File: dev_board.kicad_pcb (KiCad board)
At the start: 2 copper layers, 29 parts, among them J3 Conn_02x10_Odd_Even, J4 Conn_02x10_Odd_Even, U1 93LCxxB, U2 LT8609, U3 KSZ8081RND

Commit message: a bunch of stuff I guess. mostly layout.
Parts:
- removed C1: 1uF, Capacitors_SMD:C_0603
- added C13: 0.1u, Capacitors_SMD:C_0603, F.Cu at (30.7, 102.0)
- added C14: 0.1u, Capacitors_SMD:C_0603, F.Cu at (79.2, 114.9)
- added C15: 22u, Capacitors_SMD:C_0603, F.Cu at (91.3, 85.5)
- added C16: 0.1u, Capacitors_SMD:C_0603, F.Cu at (82.1, 123.7)
- added C17: C_Small, Capacitors_SMD:C_0603, F.Cu at (123.4, 119.4)
- added C18: C_Small, Capacitors_SMD:C_0603, F.Cu at (121.9, 119.4)
- added C19: C_Small, Capacitors_SMD:C_0603, F.Cu at (122.7, 111.1)
- added C20: C_Small, Capacitors_SMD:C_0603, F.Cu at (122.8, 105.9)
- added C21: C_Small, Capacitors_SMD:C_0603, F.Cu at (114.8, 108.6)
- added C22: C_Small, Capacitors_SMD:C_0603, F.Cu at (110.8, 108.5)
- added C23: 100nF, Capacitors_SMD:C_0603, F.Cu at (83.9, 111.9)
- added C24: 100nF, Capacitors_SMD:C_0603, F.Cu at (79.5, 108.8)
- added C25: 100nF, Capacitors_SMD:C_0603, F.Cu at (85.3, 111.9)
- added C26: 100nF, Capacitors_SMD:C_0603, F.Cu at (80.4, 103.2)
- added C27: 100nF, Capacitors_SMD:C_0603, F.Cu at (92.5, 100.3)
- added C28: 4.7uF, Capacitors_SMD:C_0603, F.Cu at (83.9, 109.0)
- added C29: 10nF, Capacitors_SMD:C_0603, F.Cu at (82.6, 99.6)
- added C30: 1uF, Capacitors_SMD:C_0603, F.Cu at (85.3, 109.0)
- added C31: C_Small, Capacitors_SMD:C_0603, F.Cu at (85.7, 100.2)
- added C32: C_Small, Capacitors_SMD:C_0603, F.Cu at (93.6, 137.6)
- added J1: USB_B_Micro, Connectors_USB:USB_Micro-B_Molex-105017-0001, F.Cu at (111.9, 98.5)
- added J2: ARJ-169, Exodus_Connectors:ARJ-169, F.Cu at (38.3, 88.6)
- added L3: Ferrite_Bead_Small, Inductors_SMD:L_0603, F.Cu at (114.8, 106.9)
- added L4: Ferrite_Bead_Small, Inductors_SMD:L_0603, F.Cu at (110.8, 106.8)
- added R12: 1M DNP, Resistors_SMD:R_0603, F.Cu at (30.5, 103.4)
- added R13: 6.49K 1%, Resistors_SMD:R_0603, F.Cu at (89.9, 85.3)
- added R14: R_Small, Resistors_SMD:R_0603, F.Cu at (119.8, 116.4)
- added R15: R_Small, Resistors_SMD:R_0603, F.Cu at (114.0, 122.7)
- added R16: R_Small, Resistors_SMD:R_0603, F.Cu at (114.8, 105.3)
- added SW1: SW_Push, Buttons_Switches_SMD:SW_SPST_EVPBF, F.Cu at (82.3, 85.7)
- added U4: FT232H, Housings_QFP:LQFP-48_7x7mm_Pitch0.5mm, F.Cu at (112.3, 115.6)
- added U5: STM32F107RCTx, Housings_QFP:LQFP-64_10x10mm_Pitch0.5mm, F.Cu at (69.9, 107.6)
- C10: value 0.1u -> 47u
- C12: value 0.1u -> 22u
- C2: value 4.7uF -> 1uF
- C3: value 10nF -> C_Small
- C5: value 10pF -> 0.1uF
- C6: value 22uF -> 2.2u
- C7: value 22u -> 330p
- L1: value 2.2uH -> 1u; footprint Inductors_SMD:L_Vishay_IHLP-2020 -> Inductors_SMD:L_Vishay_IHLP-1616
- R1: value 18.2k -> 10k
- R10: value 10K -> 1K
- R11: value 1M DNP -> 10K
- R2: value 309k -> 20k
- R3: value 1M -> 324k
- R4: value 100k -> 115k
- R5: value 1K -> 25.5
- R6: value 1M DNP -> 1K
- R7: value 1K -> 1M DNP
- R8: value 10K DNP -> 1K
- R9: value 1K -> 10K DNP
- U1: value 93LCxxB -> LTC3604_UD; footprint Housings_QFP:LQFP-52_10x10mm_Pitch0.65mm -> Housings_DFN_QFN:QFN-16-1EP_3x3mm_Pitch0.5mm_ThermalVias
- U2: value LT8609 -> KSZ8081RND; footprint Housings_SSOP:MSOP-10-1EP_3x3mm_Pitch0.5mm -> Housings_DFN_QFN:QFN-24-1EP_4x4mm_Pitch0.5mm
- U3: value KSZ8081RND -> 93LCxxB; footprint Housings_DFN_QFN:QFN-20-1EP_4x4mm_Pitch0.5mm -> Housings_SOIC:SOIC-8_3.9x4.9mm_Pitch1.27mm
- moved J3 126.4 mm to (36.4, 109.7)
- moved R6 107.5 mm to (59.6, 85.6)
- moved R7 96.3 mm to (72.1, 90.0)
- moved R9 95.6 mm to (69.5, 87.9)
- moved C12 90.3 mm to (59.2, 96.8)
- moved R11 88.0 mm to (71.8, 94.0)
- moved R10 85.5 mm to (73.7, 87.4)
- moved C11 84.5 mm to (59.4, 93.1)
- moved R8 80.9 mm to (59.1, 107.2)
- moved R3 65.4 mm to (130.3, 57.5)
- moved C3 65.3 mm to (62.4, 130.8), turned to 90 degrees
- moved C5 60.1 mm to (71.6, 132.2), turned to 180 degrees
- moved R1 58.8 mm to (67.7, 127.3), turned to 90 degrees
- moved R5 57.8 mm to (130.3, 56.0)
- moved C6 57.5 mm to (133.3, 60.7)
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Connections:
- net /ethernet_phy_ksz8081/TXP renamed Net-(U3-Pad6)
- net Net-(U1-Pad2) renamed /power_supply/PGOOD
- C10 pad 1: /ethernet_phy_ksz8081/1.2V_INTERNALLY_REGULATED -> +3V3
- C11 pad 1: +3V3 -> /ethernet_phy_ksz8081/3.3V_QUIET
- C12 pad 1: +3V3 -> /ethernet_phy_ksz8081/1.2V_INTERNALLY_REGULATED
- C2 pad 1: +5V -> GND
- C2 pad 2: GND -> +5V
- C3 pad 1: Net-(C3-Pad1) -> /NRST
- C4 pad 2: Net-(C4-Pad2) -> GND
- C5 pad 1: +3V3 -> Net-(C5-Pad1)
- C5 pad 2: Net-(C5-Pad2) -> GND
- C6 pad 1: +3V3 -> /power_supply/INTVcc
- C7 pad 1: /ethernet_phy_ksz8081/3.3V_QUIET -> Net-(C7-Pad1)
- C8 pad 1: /ethernet_phy_ksz8081/1.2V_INTERNALLY_REGULATED -> +5V
- C9 pad 1: /ethernet_phy_ksz8081/3.3V_QUIET -> /power_supply/BST
- C9 pad 2: GND -> /power_supply/SW
- J3 pad 1: Net-(J3-Pad1) -> +3V3
- J3 pad 2: Net-(J3-Pad2) -> +5V
- J3 pad 3: Net-(J3-Pad3) -> GND
- J3 pad 4: Net-(J3-Pad4) -> GND
- J4 pad 1: Net-(J4-Pad1) -> +3V3
- J4 pad 2: Net-(J4-Pad2) -> +5V
- J4 pad 3: Net-(J4-Pad3) -> GND
- J4 pad 4: Net-(J4-Pad4) -> GND
- L1 pad 1: Net-(C4-Pad1) -> /power_supply/SW
- R1 pad 1: Net-(R1-Pad1) -> +3V3
- R1 pad 2: GND -> /NRST
- R10 pad 1: /ethernet_phy_ksz8081/RMII_RXER -> /stm32f107/ETH_RMII_CRS_DV
- R11 pad 1: /ethernet_phy_ksz8081/RMII_TXEN -> /ethernet_phy_ksz8081/RMII_RXER
- R2 pad 1: Net-(C5-Pad2) -> /power_supply/ITH
- R2 pad 2: GND -> Net-(C7-Pad1)
- R3 pad 1: +3V3 -> /power_supply/RT
- R3 pad 2: Net-(C5-Pad2) -> GND
- R4 pad 2: /power_supply/P_GOOD -> /power_supply/FB
- R5 pad 1: +3V3 -> /power_supply/FB
- R5 pad 2: /ethernet_phy_ksz8081/RMII_MDIO -> GND
- R6 pad 2: /ethernet_phy_ksz8081/RMII_MDC -> /stm32f107/ETH_RMII_MDIO
- R7 pad 2: /ethernet_phy_ksz8081/INTRP -> /stm32f107/ETH_RMII_MDC
- R8 pad 2: /NRST -> /ethernet_phy_ksz8081/INTRP
- R9 pad 1: /ethernet_phy_ksz8081/RMII_CRS_DV -> +3V3
- R9 pad 2: GND -> /NRST
- U1 pad 10: (no net) -> /power_supply/RT
- U1 pad 11: (no net) -> /power_supply/FB
- U1 pad 12: (no net) -> /power_supply/ITH
- U1 pad 13: (no net) -> Net-(U1-Pad13)
- U1 pad 14: (no net) -> +5V
- U1 pad 15: (no net) -> +5V
- U1 pad 16: (no net) -> +5V
- U1 pad 17: (no net) -> GND
- U1 pad 3: Net-(R14-Pad1) -> /power_supply/SW
- U1 pad 4: Net-(R14-Pad2) -> /power_supply/SW
- U1 pad 5: GND -> Net-(U1-Pad5)
- U1 pad 6: Net-(U1-Pad6) -> /power_supply/BST
- U1 pad 7: Net-(U1-Pad7) -> /power_supply/INTVcc
- U1 pad 9: (no net) -> GND
- U2 pad 1: Net-(C4-Pad2) -> /ethernet_phy_ksz8081/1.2V_INTERNALLY_REGULATED
- U2 pad 10: +5V -> /stm32f107/ETH_RMII_MDIO
- U2 pad 11: GND -> /stm32f107/ETH_RMII_MDC
- U2 pad 2: Net-(C4-Pad1) -> /ethernet_phy_ksz8081/3.3V_QUIET
- U2 pad 3: Net-(C1-Pad1) -> /RXM
- U2 pad 4: Net-(R1-Pad1) -> /RXP
- U2 pad 5: Net-(U2-Pad5) -> /TXM
- U2 pad 6: Net-(C5-Pad2) -> /TXP
- U2 pad 7: Net-(C3-Pad1) -> /ethernet_phy_ksz8081/OSC_OUT
- U2 pad 8: /power_supply/P_GOOD -> /stm32f107/MCO
- U2 pad 9: +5V -> /ethernet_phy_ksz8081/PHY_REF_RES
- U3 pad 1: /ethernet_phy_ksz8081/1.2V_INTERNALLY_REGULATED -> Net-(U3-Pad1)
- U3 pad 2: /ethernet_phy_ksz8081/3.3V_QUIET -> Net-(U3-Pad2)
- U3 pad 3: /ethernet_phy_ksz8081/RXM -> Net-(R14-Pad1)
- U3 pad 4: /ethernet_phy_ksz8081/RXP -> Net-(R14-Pad2)
- U3 pad 5: /ethernet_phy_ksz8081/TXM -> GND
- U3 pad 7: /ethernet_phy_ksz8081/OSC_OUT -> Net-(U3-Pad7)
- U3 pad 8: /ethernet_phy_ksz8081/REF_CLK_50MHZ -> +3V3
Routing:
- net +1V8: track 0.00 -> 10.3 mm
- net Net-(C20-Pad1): track 0.00 -> 10.2 mm
- net Net-(C19-Pad1): track 0.00 -> 8.61 mm
- net Net-(C18-Pad1): track 0.00 -> 8.00 mm
- net Net-(R14-Pad1): track 0.00 -> 5.89 mm
- net +3V3: track 0.00 -> 5.79 mm
- net Net-(C22-Pad1): track 0.00 -> 4.42 mm
- net Net-(C21-Pad2): track 0.00 -> 4.30 mm
- net Net-(U3-Pad1): track 0.00 -> 3.96 mm
- net Net-(U3-Pad2): track 0.00 -> 3.75 mm
- net Net-(R14-Pad2): track 0.00 -> 2.62 mm
- net Net-(R15-Pad1): track 0.00 -> 2.04 mm
- net /power_supply/RT: track 0.00 -> 1.74 mm
- net +5V: track 0.00 -> 1.00 mm
- net /USB_PROG_D+: track 0.00 -> 0.97 mm
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- added copper zone on F.Cu, net +3V3
- added copper zone on F.Cu, net +5V
- added copper zone on F.Cu, net /power_supply/BST
- added copper zone on F.Cu, net /power_supply/FB
- added copper zone on F.Cu, net /power_supply/INTVcc
- added copper zone on F.Cu, net /power_supply/ITH
- added copper zone on F.Cu, net /power_supply/SW
- added copper zone on B.Cu, net GND
- added copper zone on F.Cu, net GND
- added copper zone on F.Cu, net Net-(C7-Pad1)
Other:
- board outline added: 76.2 x 58.4 mm
- net class Default: clearance 0.2 -> 0.1524; trace_width 0.25 -> 0.1524; via_dia 0.8 -> 0.6858; via_drill 0.4 -> 0.3302
- rule pad_to_mask_clearance: 0.2 -> 0.0508
- rule trace_clearance: 0.2 -> 0.1524
- rule trace_min: 0.2 -> 0.1524
- rule via_min_drill: 0.3 -> 0.254
- rule via_min_size: 0.4 -> 0.508

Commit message: more layout
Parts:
- moved J3 110.2 mm to (144.5, 87.6)
- moved C13 53.3 mm to (77.0, 128.3)
- moved R12 53.3 mm to (76.8, 129.7)
- moved U2 38.4 mm to (76.9, 109.8), turned to 270 degrees
- moved J2 38.3 mm to (76.2, 83.2), turned to 180 degrees
- moved R13 36.8 mm to (68.5, 115.3)
- moved C15 36.8 mm to (69.9, 115.4)
- moved U1 31.1 mm to (118.8, 90.0)
- moved C10 31.1 mm to (123.3, 101.0)
- moved L1 31.1 mm to (123.7, 96.4)
- moved C6 31.1 mm to (123.1, 90.0)
- moved C7 31.1 mm to (116.9, 85.3)
- moved C8 31.1 mm to (116.8, 93.1)
- moved R2 31.1 mm to (117.0, 86.9)
- moved C9 31.1 mm to (122.4, 92.2)
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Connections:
- net /RXM renamed /RX_N
- net /RXP renamed /RX_P
- net /TXM renamed /TX_N
- net /TXP renamed /TX_P
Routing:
- net /stm32f107/ETH_RMII_TXD1: track 0.00 -> 14.7 mm
- net /stm32f107/ETH_RMII_TXD0: track 0.00 -> 13.6 mm
- net /TX_P: track 0.00 -> 11.3 mm
- net /RX_N: track 0.00 -> 11.2 mm
- net /stm32f107/ETH_RMII_TX_EN: track 0.00 -> 10.7 mm, vias 0 -> 2
- net /TX_N: track 0.00 -> 10.7 mm
- net /RX_P: track 0.00 -> 10.5 mm
- net /USB_PROG_D-: track 0.76 -> 10.4 mm
- net /USB_PROG_D+: track 0.97 -> 10.5 mm
- net Net-(R16-Pad1): track 0.00 -> 6.60 mm
- net +3V3: track 5.79 -> 2.85 mm
- net /stm32f107/ETH_RMII_RXD0: track 0.65 -> 0.00 mm

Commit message: layout
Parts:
- removed C2: 1uF, Capacitors_SMD:C_0603
- added L2: Ferrite_Bead, Inductors_SMD:L_0603, F.Cu at (82.2, 104.8)
- moved C3 48.5 mm to (87.6, 90.0), turned to 270 degrees
- moved R1 43.7 mm to (89.1, 89.8)
- moved C32 40.9 mm to (96.3, 96.8)
- moved C23 35.8 mm to (100.4, 100.6), turned to 180 degrees
- moved R10 34.6 mm to (77.5, 114.9), turned to 270 degrees
- moved C5 34.3 mm to (66.5, 98.3), turned to 270 degrees
- moved R7 33.4 mm to (70.8, 110.5)
- moved C28 31.8 mm to (100.4, 102.1), turned to 180 degrees
- moved C30 30.8 mm to (93.3, 101.0), turned to 90 degrees
- moved C4 30.6 mm to (85.7, 98.2), turned to 270 degrees
- moved C14 29.6 mm to (81.8, 107.8), turned to 0 degrees
- moved R11 27.3 mm to (79.1, 114.9), turned to 270 degrees
- moved C31 26.9 mm to (98.0, 96.8), turned to 90 degrees
- moved C12 26.2 mm to (81.8, 106.4)
- moved R8 26.0 mm to (80.6, 114.9), turned to 90 degrees
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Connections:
- J2 pad U2: /stm32f107/OTG_FS_DP -> /stm32f107/OTG_FS_N
- J2 pad U3: /stm32f107/OTG_FS_DM -> /stm32f107/OTG_FS_P
- U5 pad 44: /stm32f107/OTG_FS_DM -> /stm32f107/OTG_FS_N
- U5 pad 45: /stm32f107/OTG_FS_DP -> /stm32f107/OTG_FS_P
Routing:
- net GND: track 0.00 -> 81.1 mm, vias 24 -> 65
- net Net-(J2-PadSH1): track 0.00 -> 36.9 mm
- net /stm32f107/OTG_FS_P: track 0.00 -> 36.4 mm
- net /stm32f107/OTG_FS_N: track 0.00 -> 35.8 mm
- net /NRST: track 0.00 -> 30.0 mm
- net +3V3: track 2.85 -> 30.1 mm
- net /USB_PROG_D+: track 10.5 -> 28.7 mm
- net /USB_PROG_D-: track 10.4 -> 28.3 mm
- net /TDO: track 0.00 -> 14.2 mm
- net /TMS: track 0.00 -> 12.3 mm
- net /TDI: track 0.00 -> 11.2 mm
- net +5V: track 1.00 -> 10.6 mm
- net /TCK: track 0.00 -> 8.11 mm
- net /stm32f107/ETH_RMII_TX_EN: track 10.7 -> 3.38 mm, vias 2 -> 0
- net /stm32f107/OSC1: track 0.00 -> 7.04 mm
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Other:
- board size 76.2 x 58.4 mm -> 76.3 x 43.7 mm

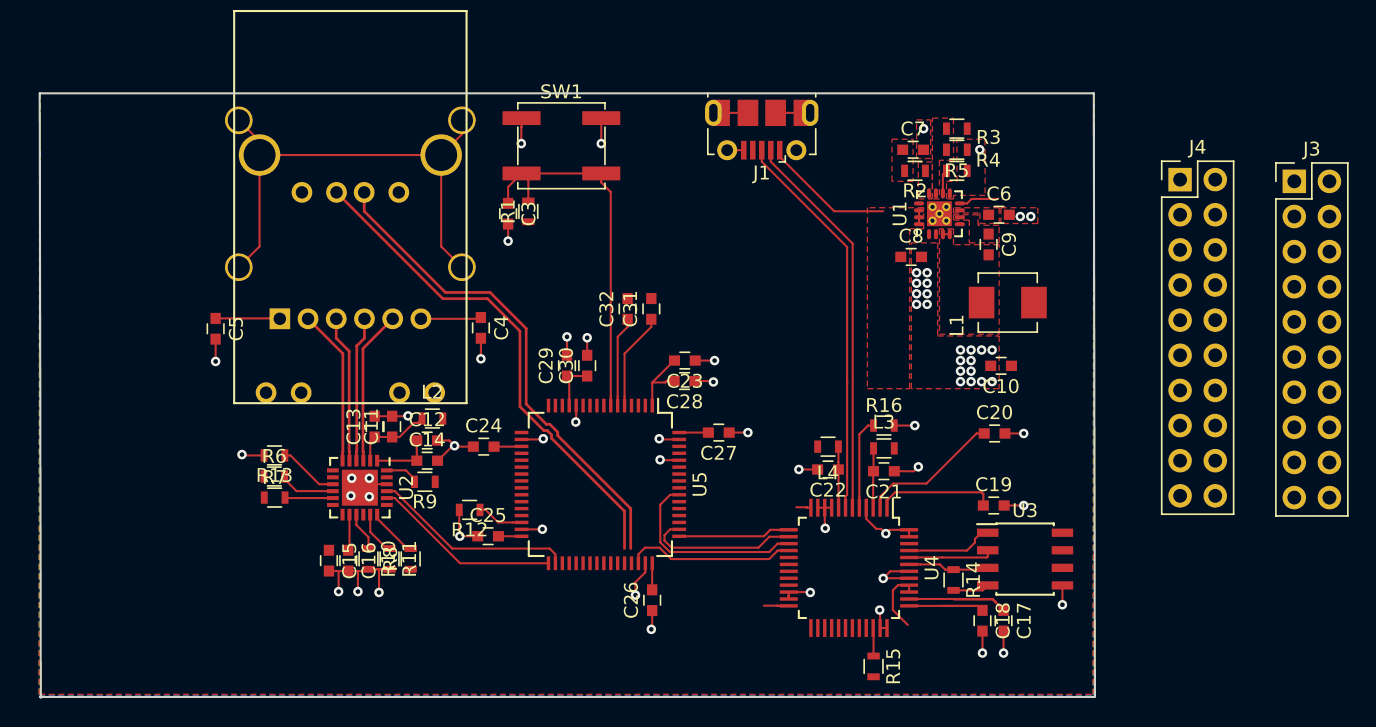
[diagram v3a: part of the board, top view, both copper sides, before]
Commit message: updated power supply circuit. Better bandwidth, added softstart cap
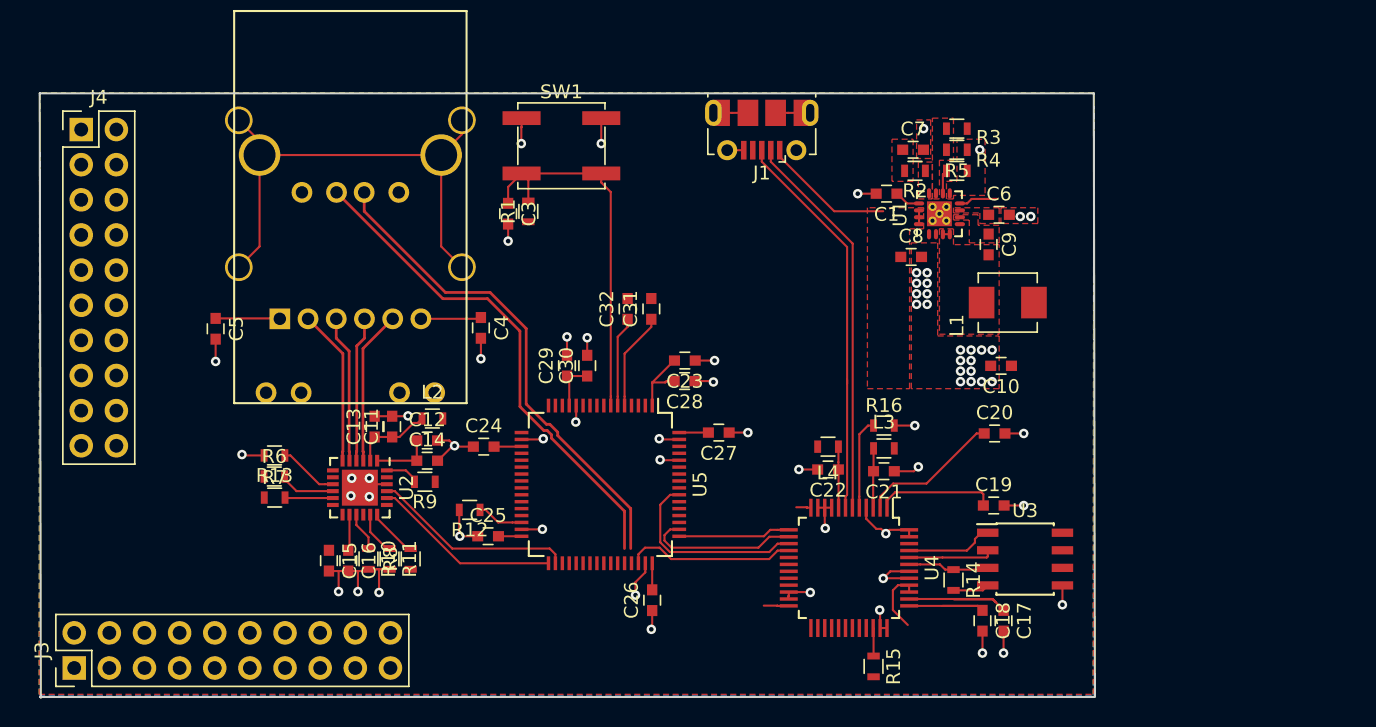
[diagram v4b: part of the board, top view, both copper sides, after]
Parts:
- added C1: 2200p, Capacitors_SMD:C_0603, F.Cu at (115.0, 88.5)
- L1: value 1u -> 0.47u
- R3: value 324k -> 210k
- moved J3 95.0 mm to (56.3, 122.8), turned to 90 degrees
- moved J4 79.5 mm to (56.8, 83.9)
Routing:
- net Net-(C1-Pad1): track 0.00 -> 1.89 mm
- net GND: track 81.1 -> 82.5 mm, vias 65 -> 66

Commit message: some layout changes? picked some random oscillator packages.
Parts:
- added Y1: Crystal, Crystals:Crystal_SMD_0603-4pin_6.0x3.5mm_HandSoldering, F.Cu at (137.1, 106.2)
- added Y2: Crystal, Crystals:Crystal_SMD_0603-4pin_6.0x3.5mm_HandSoldering, F.Cu at (103.5, 96.2)
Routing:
- net +5V: track 10.6 -> 34.4 mm
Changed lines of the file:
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@@
     (thickness 1.6)
     (drawings 4)
-    (tracks 403)
+    (tracks 407)
     (zones 0)
-    (modules 61)
+    (modules 63)
     (nets 148)
   )
@@
     (add_net "Net-(U3-Pad7)")
   )
+  (module Crystals:Crystal_SMD_0603-4pin_6.0x3.5mm_HandSoldering (layer F.Cu)
+    (at 103.488 96.2285 180)
+    (descr "SMD Crystal SERIES SMD0603/4 http://www.petermann-technik.de/fileadmin/petermann/pdf/SMD0603-4.pdf, hand-soldering, 6.0x3.5mm^2 package")
+    (tags "SMD SMT crystal hand-soldering")
+    (attr smd)
+    (fp_text reference Y2 (at 0 -3.6 180) (layer F.SilkS)
+      (effects (font (size 1 1) (thickness 0.15)))
+    )
+    (fp_text value Crystal (at 0 3.6 180) (layer F.Fab)
+      (effects (font (size 1 1) (thickness 0.15)))
+    )
+    (fp_text user %R (at 0 0 180) (layer F.Fab)
+      (effects (font (size 1 1) (thickness 0.15)))
+    )
+    (fp_line (start -2.9 -1.75) (end 2.9 -1.75) (layer F.Fab) (width 0.1))
+    (fp_line (start 2.9 -1.75) (end 3 -1.65) (layer F.Fab) (width 0.1))
+    (fp_line (start 3 -1.65) (end 3 1.65) (layer F.Fab) (width 0.1))
+    (fp_line (start 3 1.65) (end 2.9 1.75) (layer F.Fab) (width 0.1))
+    (fp_line (start 2.9 1.75) (end -2.9 1.75) (layer F.Fab) (width 0.1))
+    (fp_line (start -2.9 1.75) (end -3 1.65) (layer F.Fab) (width 0.1))
+    (fp_line (start -3 1.65) (end -3 -1.65) (layer F.Fab) (width 0.1))
+    (fp_line (start -3 -1.65) (end -2.9 -1.75) (layer F.Fab) (width 0.1))
+    (fp_line (start -3 0.75) (end -2 1.75) (layer F.Fab) (width 0.1))
+    (fp_line (start -4.2 0.3) (end -3.2 0.3) (layer F.SilkS) (width 0.12))
+    (fp_line (start -3.2 0.3) (end -3.2 -0.3) (layer F.SilkS) (width 0.12))
+    (fp_line (start 3.2 -0.3) (end 3.2 0.3) (layer F.SilkS) (width 0.12))
+    (fp_line (start -1.1 -1.95) (end 1.1 -1.95) (layer F.SilkS) (width 0.12))
+    (fp_line (start 1.1 1.95) (end -1.1 1.95) (layer F.SilkS) (width 0.12))
+    (fp_line (start -1.1 1.95) (end -1.1 2.8) (layer F.SilkS) (width 0.12))
+    (fp_line (start -4.3 -2.9) (end -4.3 2.9) (layer F.CrtYd) (width 0.05))
+    (fp_line (start -4.3 2.9) (end 4.3 2.9) (layer F.CrtYd) (width 0.05))
+    (fp_line (start 4.3 2.9) (end 4.3 -2.9) (layer F.CrtYd) (width 0.05))
+    (fp_line (start 4.3 -2.9) (end -4.3 -2.9) (layer F.CrtYd) (width 0.05))
+    (fp_circle (center 0 0) (end 0.4 0) (layer F.Adhes) (width 0.1))
+    (fp_circle (center 0 0) (end 0.333333 0) (layer F.Adhes) (width 0.133333))
+    (fp_circle (center 0 0) (end 0.213333 0) (layer F.Adhes) (width 0.133333))
+    (fp_circle (center 0 0) (end 0.093333 0) (layer F.Adhes) (width 0.186667))
+    (pad 1 smd rect (at -2.65 1.55 180) (size 2.7 2.1) (layers F.Cu F.Paste F.Mask)
+      (net 118 /stm32f107/OSC1))
+    (pad 2 smd rect (at 2.65 1.55 180) (size 2.7 2.1) (layers F.Cu F.Paste F.Mask)
+      (net 117 /stm32f107/OSC2))
+    (pad 3 smd rect (at 2.65 -1.55 180) (size 2.7 2.1) (layers F.Cu F.Paste F.Mask))
+    (pad 4 smd rect (at -2.65 -1.55 180) (size 2.7 2.1) (layers F.Cu F.Paste F.Mask))
+    (model ${KISYS3DMOD}/Crystals.3dshapes/Crystal_SMD_0603-4pin_6.0x3.5mm_HandSoldering.wrl
+      (at (xyz 0 0 0))
+      (scale (xyz 1 1 1))
+      (rotate (xyz 0 0 0))
+    )
+  )
+  (module Crystals:Crystal_SMD_0603-4pin_6.0x3.5mm_HandSoldering (layer F.Cu)
+    (at 137.0965 106.2355 90)
+    (descr "SMD Crystal SERIES SMD0603/4 http://www.petermann-technik.de/fileadmin/petermann/pdf/SMD0603-4.pdf, hand-soldering, 6.0x3.5mm^2 package")
+    (tags "SMD SMT crystal hand-soldering")
+    (attr smd)
+    (fp_text reference Y1 (at 0 -3.6 90) (layer F.SilkS)
+      (effects (font (size 1 1) (thickness 0.15)))
+    )
+    (fp_text value Crystal (at 0 3.6 90) (layer F.Fab)
+      (effects (font (size 1 1) (thickness 0.15)))
+    )
+    (fp_circle (center 0 0) (end 0.093333 0) (layer F.Adhes) (width 0.186667))
+    (fp_circle (center 0 0) (end 0.213333 0) (layer F.Adhes) (width 0.133333))
+    (fp_circle (center 0 0) (end 0.333333 0) (layer F.Adhes) (width 0.133333))
+    (fp_circle (center 0 0) (end 0.4 0) (layer F.Adhes) (width 0.1))
+    (fp_line (start 4.3 -2.9) (end -4.3 -2.9) (layer F.CrtYd) (width 0.05))
+    (fp_line (start 4.3 2.9) (end 4.3 -2.9) (layer F.CrtYd) (width 0.05))
+    (fp_line (start -4.3 2.9) (end 4.3 2.9) (layer F.CrtYd) (width 0.05))
+    (fp_line (start -4.3 -2.9) (end -4.3 2.9) (layer F.CrtYd) (width 0.05))
+    (fp_line (start -1.1 1.95) (end -1.1 2.8) (layer F.SilkS) (width 0.12))
+    (fp_line (start 1.1 1.95) (end -1.1 1.95) (layer F.SilkS) (width 0.12))
+    (fp_line (start -1.1 -1.95) (end 1.1 -1.95) (layer F.SilkS) (width 0.12))
+    (fp_line (start 3.2 -0.3) (end 3.2 0.3) (layer F.SilkS) (width 0.12))
+    (fp_line (start -3.2 0.3) (end -3.2 -0.3) (layer F.SilkS) (width 0.12))
+    (fp_line (start -4.2 0.3) (end -3.2 0.3) (layer F.SilkS) (width 0.12))
+    (fp_line (start -3 0.75) (end -2 1.75) (layer F.Fab) (width 0.1))
+    (fp_line (start -3 -1.65) (end -2.9 -1.75) (layer F.Fab) (width 0.1))
+    (fp_line (start -3 1.65) (end -3 -1.65) (layer F.Fab) (width 0.1))
+    (fp_line (start -2.9 1.75) (end -3 1.65) (layer F.Fab) (width 0.1))
+    (fp_line (start 2.9 1.75) (end -2.9 1.75) (layer F.Fab) (width 0.1))
+    (fp_line (start 3 1.65) (end 2.9 1.75) (layer F.Fab) (width 0.1))
+    (fp_line (start 3 -1.65) (end 3 1.65) (layer F.Fab) (width 0.1))
+    (fp_line (start 2.9 -1.75) (end 3 -1.65) (layer F.Fab) (width 0.1))
+    (fp_line (start -2.9 -1.75) (end 2.9 -1.75) (layer F.Fab) (width 0.1))
+    (fp_text user %R (at 0 0 90) (layer F.Fab)
+      (effects (font (size 1 1) (thickness 0.15)))
+    )
+    (pad 4 smd rect (at -2.65 -1.55 90) (size 2.7 2.1) (layers F.Cu F.Paste F.Mask))
+    (pad 3 smd rect (at 2.65 -1.55 90) (size 2.7 2.1) (layers F.Cu F.Paste F.Mask))
+    (pad 2 smd rect (at 2.65 1.55 90) (size 2.7 2.1) (layers F.Cu F.Paste F.Mask)
+      (net 97 "Net-(C20-Pad1)"))
+    (pad 1 smd rect (at -2.65 1.55 90) (size 2.7 2.1) (layers F.Cu F.Paste F.Mask)
+      (net 113 "Net-(C19-Pad1)"))
+    (model ${KISYS3DMOD}/Crystals.3dshapes/Crystal_SMD_0603-4pin_6.0x3.5mm_HandSoldering.wrl
+      (at (xyz 0 0 0))
+      (scale (xyz 1 1 1))
+      (rotate (xyz 0 0 0))
+    )
+  )
   (module Capacitors_SMD:C_0603 (layer F.Cu)
     (at 114.9865 88.519 180)
@@
   (segment (start 107.2655 85.377) (end 107.2655 85.852) (width 0.1524) (layer F.Cu) (net 39))
   (segment (start 111.2025 89.789) (end 114.7445 89.789) (width 0.1524) (layer F.Cu) (net 39))
+  (segment (start 60.511081 83.8835) (end 66.861081 90.2335) (width 0.1524) (layer B.Cu) (net 39))
+  (segment (start 59.309 83.8835) (end 60.511081 83.8835) (width 0.1524) (layer B.Cu) (net 39))
+  (segment (start 77.916 90.2335) (end 79.7245 88.425) (width 0.1524) (layer B.Cu) (net 39))
+  (segment (start 66.861081 90.2335) (end 77.916 90.2335) (width 0.1524) (layer B.Cu) (net 39))
   (segment (start 74.3831 109.523) (end 74.9605 109.523) (width 0.1524) (layer F.Cu) (net 41))
   (segment (start 73.9724 109.523) (end 74.3831 109.523) (width 0.1524) (layer F.Cu) (net 41))
